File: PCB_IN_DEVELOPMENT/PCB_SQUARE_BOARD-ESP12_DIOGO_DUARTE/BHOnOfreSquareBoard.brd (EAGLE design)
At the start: 47.6 x 47.7 mm, 23 parts, among them J1 4p, J6 8p, J7 8p, K1 OMRON-G3MB-202P-SSR2, K2 OMRON-G3MB-202P-SSR2, Q1 S8050, Q2 S8050, U1 LM1117, U2 esp12

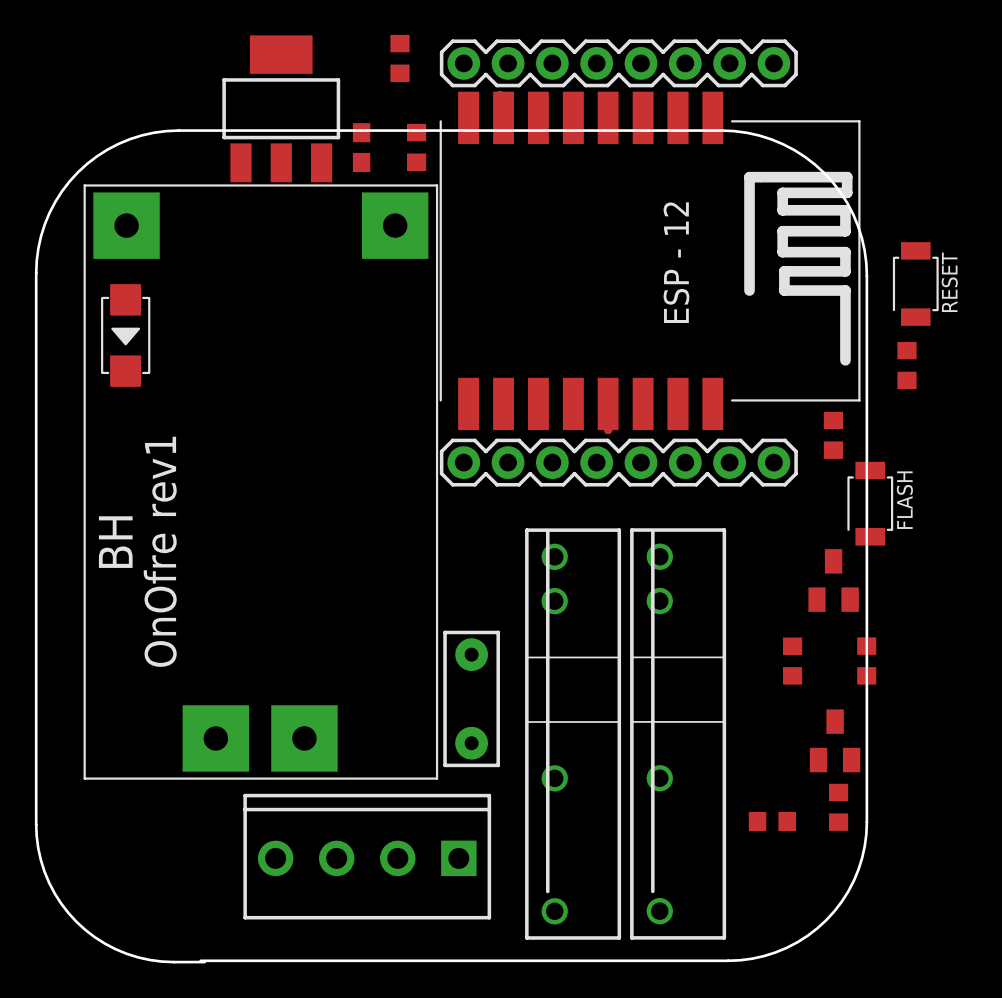
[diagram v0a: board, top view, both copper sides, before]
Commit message: Routing with Mains isolation :)
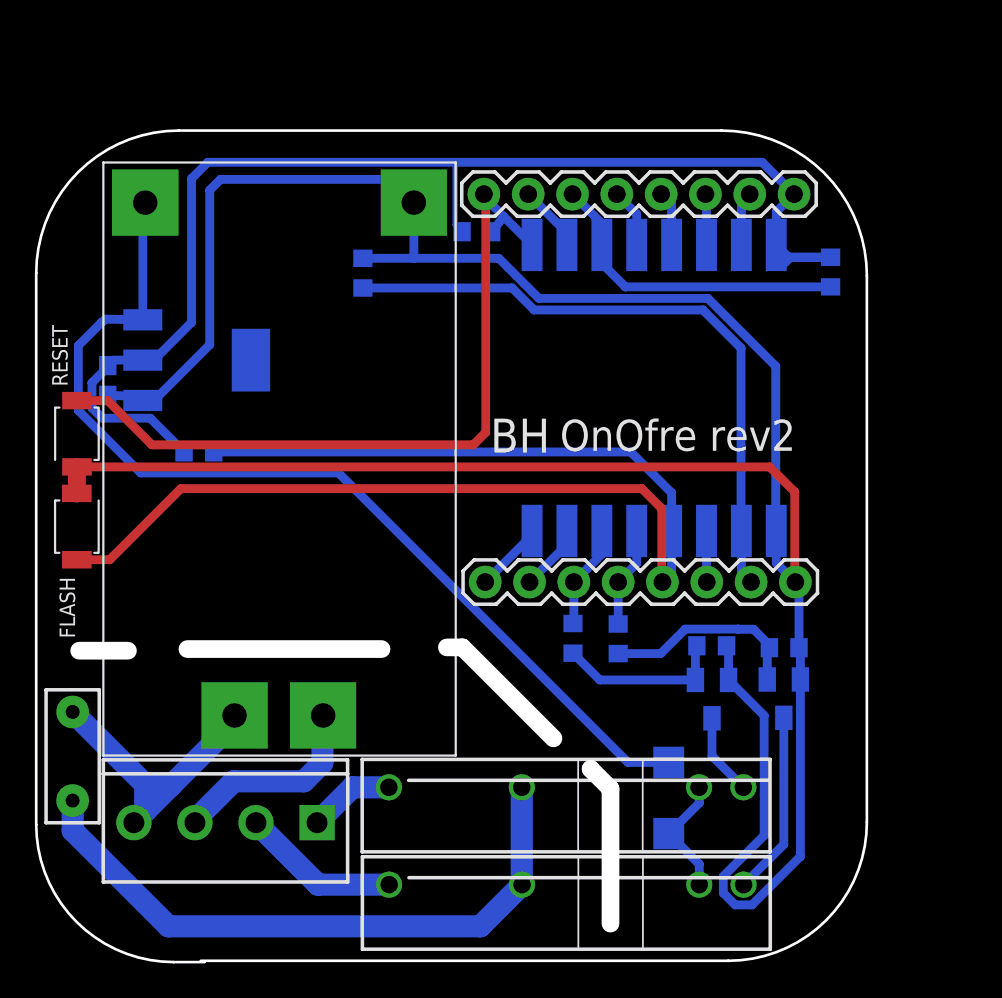
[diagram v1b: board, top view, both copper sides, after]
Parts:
- moved RESET 48.8 mm to (2.33, 30.2)
- moved FLASH 45.5 mm to (2.33, 24.9), turned to 90 degrees
- moved D3 40.9 mm to (36.3, 9.33), flipped to the bottom
- moved R8 36.4 mm to (9.32, 29.2), flipped to the bottom, turned to 0 degrees
- moved F1 23.1 mm to (2.09, 11.7)
- moved J7 20.4 mm to (43.4, 43.9), turned to 180 degrees
- moved J6 20.2 mm to (43.5, 21.7), turned to 180 degrees
- moved C4 19.7 mm to (4.10, 33.3), flipped to the bottom
- moved R1 16.9 mm to (30.8, 18.5), flipped to the bottom, turned to 270 degrees
- moved U1 15.2 mm to (9.21, 34.4), flipped to the bottom, turned to 90 degrees
- moved R4 13.7 mm to (33.4, 18.5), flipped to the bottom, turned to 270 degrees
- moved K1 11.6 mm to (32.9, 4.36), turned to 0 degrees
- moved R10 10.9 mm to (25.3, 41.8), flipped to the bottom, turned to 0 degrees
- moved Q2 9.74 mm to (38.7, 15.0), flipped to the bottom, turned to 180 degrees
- moved R3 9.66 mm to (42.9, 17.9), flipped to the bottom, turned to 0 degrees
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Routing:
- net GND: track 0.23 -> 157.9 mm
- net GPIO0: track 0.00 -> 73.2 mm
- net 3V3: track 0.76 -> 72.7 mm
- net VCC: track 0.00 -> 57.1 mm
- net RESET: track 0.00 -> 43.6 mm
- net GPIO15: track 0.00 -> 37.4 mm
- net NEUTRAL_IN_FUSED: track 0.00 -> 36.3 mm
- net CH_PD: track 0.00 -> 18.3 mm
- net NEUTRAL_IN: track 0.00 -> 17.4 mm
- net N$7: track 0.00 -> 11.6 mm
- net FASE: track 0.00 -> 11.5 mm
- net N$1: track 0.00 -> 10.5 mm
- net N$13: track 0.00 -> 9.65 mm
- net NEUTRAL_ONE_OUT: track 0.00 -> 9.10 mm
- net N$2: track 0.00 -> 7.04 mm
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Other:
- outline, holes or cut-outs redrawn
- board text added: "OnOfre rev2"
- board text removed: "OnOfre rev1"

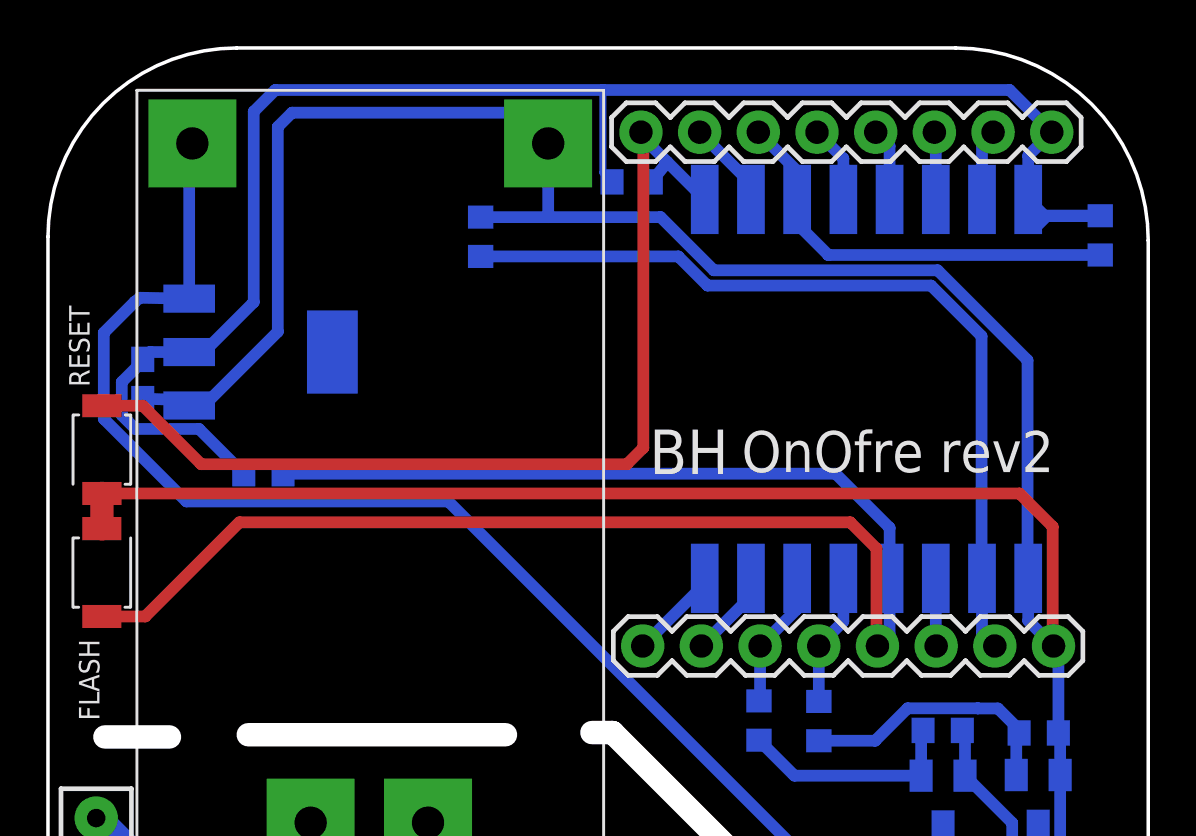
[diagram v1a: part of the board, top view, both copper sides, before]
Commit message: Cleared antenna path
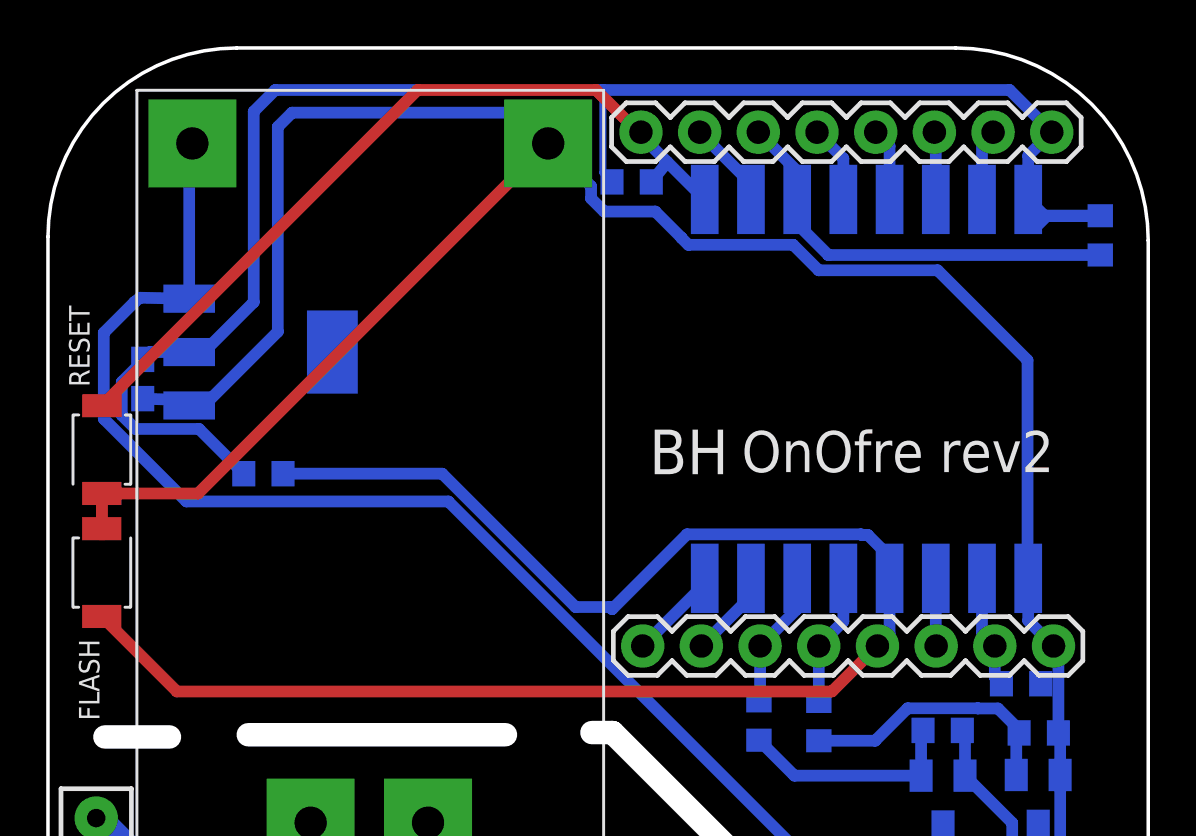
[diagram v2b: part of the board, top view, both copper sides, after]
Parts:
- moved R11 30.4 mm to (42.1, 20.1), turned to 180 degrees
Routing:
- net GPIO15: track 37.4 -> 5.87 mm
- net GND: track 157.9 -> 132.1 mm
- net RESET: track 43.6 -> 34.9 mm
- net GPIO0: track 73.2 -> 70.2 mm
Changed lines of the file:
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@@
 <attribute name="VALUE" x="29.789371875" y="41.078175" size="1.27" layer="28" rot="MR0"/>
 </element>
-<element name="R11" library="resistor" library_urn="urn:adsk.eagle:library:348" package="R0603" package3d_urn="urn:adsk.eagle:package:26057/1" value="10k" x="18.726728125" y="39.42138125" smashed="yes" rot="MR90">
-<attribute name="VALUE" x="16.1505125" y="38.02523125" size="1.27" layer="28" rot="MR90"/>
+<element name="R11" library="resistor" library_urn="urn:adsk.eagle:library:348" package="R0603" package3d_urn="urn:adsk.eagle:package:26057/1" value="10k" x="42.114084375" y="20.077509375" smashed="yes" rot="MR180">
+<attribute name="VALUE" x="37.977471875" y="20.721171875" size="1.27" layer="28" rot="MR180"/>
 </element>
 <element name="K2" library="Omron G3MB 202p SSR" package="OMRON-G3MB-202P-SSR" value="OMRON-G3MB-202P-SSR2" x="32.917278125" y="9.9453875" smashed="yes">
@@
 <wire x1="9.947346875" y1="35.313109375" x2="9.947346875" y2="44.177565625" width="0.508" layer="16"/>
 <wire x1="9.947346875" y1="44.177565625" x2="10.563165625" y2="44.793384375" width="0.508" layer="16"/>
-<wire x1="18.726728125" y1="40.27138125" x2="21.647321875" y2="40.27138125" width="0.508" layer="16"/>
-<wire x1="21.647321875" y1="40.27138125" x2="26.51653125" y2="40.27138125" width="0.508" layer="16"/>
 <wire x1="38.504609375" y1="37.970928125" x2="42.39464375" y2="34.08089375" width="0.508" layer="16"/>
-<wire x1="26.51653125" y1="40.27138125" x2="28.816984375" y2="37.970928125" width="0.508" layer="16"/>
-<wire x1="28.816984375" y1="37.970928125" x2="38.504609375" y2="37.970928125" width="0.508" layer="16"/>
 <wire x1="42.39464375" y1="34.08089375" x2="42.39464375" y2="24.668003125" width="0.508" layer="16"/>
 <wire x1="42.39464375" y1="24.668003125" x2="42.424275" y2="24.638371875" width="0.508" layer="16"/>
-<wire x1="21.648915625" y1="43.462690625" x2="21.648915625" y2="40.272975" width="0.508" layer="16"/>
-<wire x1="21.648915625" y1="40.272975" x2="21.647321875" y2="40.27138125" width="0.508" layer="16"/>
 <wire x1="2.32974375" y1="26.78851875" x2="2.334090625" y2="26.792865625" width="1.016" layer="1" curve="90"/>
-<wire x1="2.334090625" y1="26.792865625" x2="2.334090625" y2="28.311728125" width="1.016" layer="1"/>
-<wire x1="2.334090625" y1="28.311728125" x2="42.04841875" y2="28.311728125" width="0.508" layer="1"/>
-<wire x1="42.04841875" y1="28.311728125" x2="43.484115625" y2="26.87603125" width="0.508" layer="1"/>
-<wire x1="43.484115625" y1="26.87603125" x2="43.484115625" y2="21.746684375" width="0.508" layer="1"/>
-<wire x1="43.484115625" y1="21.746684375" x2="43.5195875" y2="21.7112125" width="0.508" layer="1"/>
+<wire x1="21.648915625" y1="43.462690625" x2="23.50525" y2="41.60635625" width="0.508" layer="16"/>
+<wire x1="23.50525" y1="41.60635625" x2="23.50525" y2="41.07926875" width="0.508" layer="16"/>
+<wire x1="23.50525" y1="41.07926875" x2="24.070265625" y2="40.514253125" width="0.508" layer="16"/>
+<wire x1="24.070265625" y1="40.514253125" x2="26.28701875" y2="40.514253125" width="0.508" layer="16"/>
+<wire x1="26.28701875" y1="40.514253125" x2="27.417878125" y2="39.38339375" width="0.508" layer="16"/>
+<wire x1="27.417878125" y1="39.38339375" x2="27.417878125" y2="39.370034375" width="0.508" layer="16"/>
+<wire x1="27.417878125" y1="39.370034375" x2="27.714715625" y2="39.073196875" width="0.508" layer="16"/>
+<wire x1="27.714715625" y1="39.073196875" x2="32.25199375" y2="39.073196875" width="0.508" layer="16"/>
+<wire x1="32.25199375" y1="39.073196875" x2="33.3542625" y2="37.970928125" width="0.508" layer="16"/>
+<wire x1="33.3542625" y1="37.970928125" x2="38.504609375" y2="37.970928125" width="0.508" layer="16"/>
+<wire x1="2.32974375" y1="26.78851875" x2="2.334090625" y2="26.792865625" width="0.508" layer="1"/>
+<wire x1="2.334090625" y1="26.792865625" x2="2.334090625" y2="28.311728125" width="0.508" layer="1"/>
+<wire x1="2.334090625" y1="28.311728125" x2="6.497953125" y2="28.311728125" width="0.508" layer="1"/>
+<wire x1="6.497953125" y1="28.311728125" x2="21.648915625" y2="43.462690625" width="0.508" layer="1"/>
+<wire x1="43.015471875" y1="21.500340625" x2="42.964084375" y2="20.077509375" width="0" layer="19" extent="16-16"/>
 </signal>
 <signal name="VCC">
@@
 <wire x1="36.424275" y1="23.93720625" x2="36.424275" y2="22.2359" width="0.508" layer="16"/>
 <wire x1="36.424275" y1="22.2359" x2="35.8995875" y2="21.7112125" width="0.508" layer="16"/>
-<wire x1="10.174078125" y1="29.16829375" x2="34.086575" y2="29.16829375" width="0.508" layer="16"/>
-<wire x1="34.086575" y1="29.16829375" x2="36.4262375" y2="26.82863125" width="0.508" layer="16"/>
-<wire x1="36.4262375" y1="26.82863125" x2="36.4262375" y2="23.93916875" width="0.508" layer="16"/>
 <wire x1="36.4262375" y1="23.93916875" x2="36.424275" y2="23.93720625" width="0.508" layer="16"/>
-<wire x1="2.32974375" y1="22.98851875" x2="4.21234375" y2="22.98851875" width="0.508" layer="1"/>
-<wire x1="4.21234375" y1="22.98851875" x2="8.28945625" y2="27.06563125" width="0.508" layer="1"/>
-<wire x1="8.28945625" y1="27.06563125" x2="34.72020625" y2="27.06563125" width="0.508" layer="1"/>
-<wire x1="34.72020625" y1="27.06563125" x2="35.857815625" y2="25.928021875" width="0.508" layer="1"/>
-<wire x1="35.857815625" y1="25.928021875" x2="35.857815625" y2="21.752984375" width="0.508" layer="1"/>
-<wire x1="35.857815625" y1="21.752984375" x2="35.8995875" y2="21.7112125" width="0.508" layer="1"/>
+<wire x1="10.174078125" y1="29.16829375" x2="17.062971875" y2="29.16829375" width="0.508" layer="16"/>
+<wire x1="17.062971875" y1="29.16829375" x2="22.83323125" y2="23.398034375" width="0.508" layer="16"/>
+<wire x1="22.83323125" y1="23.398034375" x2="24.320415625" y2="23.398034375" width="0.508" layer="16"/>
+<wire x1="24.320415625" y1="23.398034375" x2="24.4062" y2="23.31225" width="0.508" layer="16"/>
+<wire x1="35.192609375" y1="26.544771875" x2="35.221921875" y2="26.515459375" width="0.508" layer="16"/>
+<wire x1="35.221921875" y1="26.515459375" x2="35.483771875" y2="26.515459375" width="0.508" layer="16"/>
+<wire x1="27.655940625" y1="26.544771875" x2="35.192609375" y2="26.544771875" width="0.508" layer="16"/>
+<wire x1="24.4062" y1="23.31225" x2="24.42341875" y2="23.31225" width="0.508" layer="16"/>
+<wire x1="24.42341875" y1="23.31225" x2="27.655940625" y2="26.544771875" width="0.508" layer="16"/>
+<wire x1="35.483771875" y1="26.515459375" x2="36.424275" y2="25.57495625" width="0.508" layer="16"/>
+<wire x1="36.424275" y1="25.57495625" x2="36.424275" y2="24.638371875" width="0.508" layer="16"/>
+<wire x1="2.32974375" y1="22.98851875" x2="5.5755" y2="19.7427625" width="0.508" layer="1"/>
+<wire x1="33.9311375" y1="19.7427625" x2="35.8995875" y2="21.7112125" width="0.508" layer="1"/>
+<wire x1="5.5755" y1="19.7427625" x2="33.9311375" y2="19.7427625" width="0.508" layer="1"/>
 </signal>
 <signal name="RESET">
@@
 <wire x1="25.663803125" y1="43.79884375" x2="25.663803125" y2="43.9487625" width="0.508" layer="16"/>
 <wire x1="26.111646875" y1="41.79760625" x2="26.806375" y2="42.656271875" width="0.508" layer="16"/>
-<wire x1="2.334090625" y1="32.111728125" x2="4.097690625" y2="32.111728125" width="0.508" layer="1"/>
-<wire x1="4.097690625" y1="32.111728125" x2="6.631565625" y2="29.577853125" width="0.508" layer="1"/>
-<wire x1="6.631565625" y1="29.577853125" x2="25.057359375" y2="29.577853125" width="0.508" layer="1"/>
-<wire x1="25.057359375" y1="29.577853125" x2="25.768365625" y2="30.288859375" width="0.508" layer="1"/>
-<wire x1="25.768365625" y1="30.288859375" x2="25.768365625" y2="43.8442" width="0.508" layer="1"/>
-<wire x1="25.768365625" y1="43.8442" x2="25.663803125" y2="43.9487625" width="0.508" layer="1"/>
+<wire x1="25.547575" y1="43.9487625" x2="25.663803125" y2="43.9487625" width="0.508" layer="1"/>
+<wire x1="23.72225" y1="45.7740875" x2="25.547575" y2="43.9487625" width="0.508" layer="1"/>
+<wire x1="2.334090625" y1="32.111728125" x2="15.99645" y2="45.7740875" width="0.508" layer="1"/>
+<wire x1="15.99645" y1="45.7740875" x2="23.72225" y2="45.7740875" width="0.508" layer="1"/>
 </signal>
 <signal name="CH_PD">
@@
 <wire x1="40.424275" y1="25.57728125" x2="40.424275" y2="24.980015625" width="0.508" layer="16"/>
 <wire x1="40.424275" y1="24.980015625" x2="40.424275" y2="24.638371875" width="0.508" layer="16"/>
-<wire x1="18.726728125" y1="38.57138125" x2="27.28258125" y2="38.57138125" width="0.508" layer="16"/>
-<wire x1="28.5434375" y1="37.310525" x2="38.218353125" y2="37.310525" width="0.508" layer="16"/>
-<wire x1="38.218353125" y1="37.310525" x2="40.405175" y2="35.123703125" width="0.508" layer="16"/>
-<wire x1="27.28258125" y1="38.57138125" x2="28.5434375" y2="37.310525" width="0.508" layer="16"/>
-<wire x1="40.405175" y1="35.123703125" x2="40.405175" y2="24.999115625" width="0.508" layer="16"/>
 <wire x1="40.405175" y1="24.999115625" x2="40.424275" y2="24.980015625" width="0.508" layer="16"/>
+<wire x1="41.264084375" y1="20.077509375" x2="40.9795875" y2="20.36200625" width="0.508" layer="16"/>
+<wire x1="40.9795875" y1="20.36200625" x2="40.9795875" y2="21.7112125" width="0.508" layer="16"/>
 </signal>
 <signal name="3V3">
